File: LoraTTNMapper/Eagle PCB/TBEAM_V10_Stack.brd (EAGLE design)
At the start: 100 x 80 mm, 28 parts, among them IC1 L298, IC2 ULN2003AD, J1 1X2-3.5MM, J2 1X2-3.5MM, J3 1X2-3.5MM

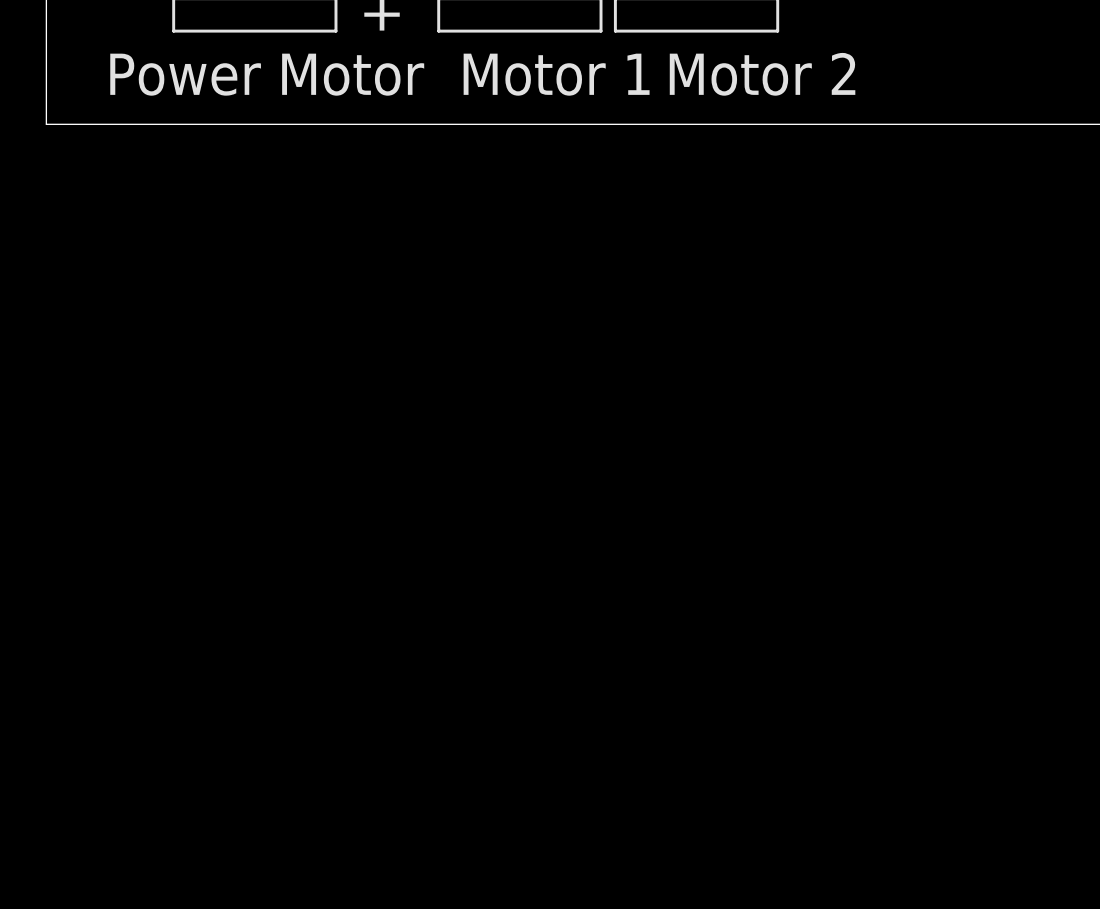
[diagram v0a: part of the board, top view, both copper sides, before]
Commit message: PCB Update P Mosfet to switch Solar Panel
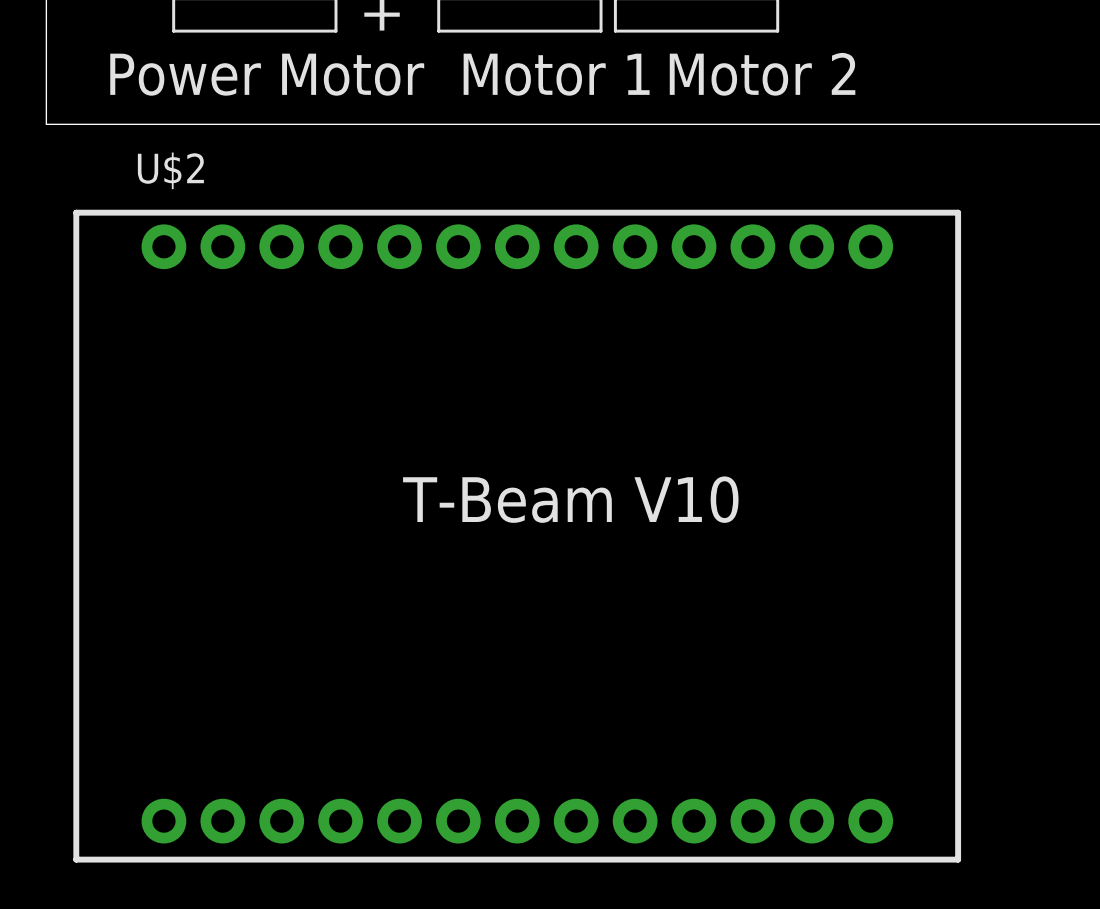
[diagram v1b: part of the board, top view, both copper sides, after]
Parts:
- added U$2: ESP32DEVKITV1, TTGO T-Beam V10:ESP32-DEVKITV1
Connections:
- net SCL: now also U$1.18; no longer U$1.17
- net SDA: now also U$1.17; no longer U$1.18
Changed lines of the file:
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@@
 <attribute name="VALUE" x="82.59" y="1.27" size="1.27" layer="27" ratio="10"/>
+</element>
+<element name="U$2" library="TTGO T-Beam V10" package="ESP32-DEVKITV1" value="ESP32DEVKITV1" x="27.94" y="-16.51" smashed="yes">
+<attribute name="NAME" x="3.81" y="-2.54" size="1.27" layer="21"/>
 </element>
 </elements>
@@
 </signal>
 <signal name="SCL">
-<contactref element="U$1" pad="17"/>
+<contactref element="U$1" pad="18"/>
 <contactref element="BME280" pad="2"/>
 <contactref element="OLED_DISPLAY" pad="3"/>
 <contactref element="INA219" pad="4"/>
+<wire x1="72.39" y1="26.67" x2="72.39" y2="35.56" width="0" layer="19" extent="1-1"/>
 <wire x1="54.61" y1="43.18" x2="72.39" y2="35.56" width="0" layer="19" extent="1-1"/>
-<wire x1="30.47" y1="74.73" x2="54.61" y2="43.18" width="0" layer="19" extent="1-1"/>
-<wire x1="72.39" y1="26.67" x2="54.61" y2="43.18" width="0" layer="19" extent="1-1"/>
+<wire x1="27.93" y1="74.73" x2="54.61" y2="43.18" width="0" layer="19" extent="1-1"/>
 </signal>
 <signal name="SDA">
-<contactref element="U$1" pad="18"/>
+<contactref element="U$1" pad="17"/>
 <contactref element="OLED_DISPLAY" pad="4"/>
 <contactref element="BME280" pad="1"/>
 <contactref element="INA219" pad="3"/>
+<wire x1="69.85" y1="26.67" x2="69.85" y2="35.56" width="0" layer="19" extent="1-1"/>
 <wire x1="57.15" y1="43.18" x2="69.85" y2="35.56" width="0" layer="19" extent="1-1"/>
-<wire x1="27.93" y1="74.73" x2="57.15" y2="43.18" width="0" layer="19" extent="1-1"/>
-<wire x1="69.85" y1="26.67" x2="57.15" y2="43.18" width="0" layer="19" extent="1-1"/>
+<wire x1="30.47" y1="74.73" x2="57.15" y2="43.18" width="0" layer="19" extent="1-1"/>
 </signal>
 <signal name="GPIO15">
